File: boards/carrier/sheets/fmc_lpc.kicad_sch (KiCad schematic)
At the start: 3 parts, among them J1 FX10A-168P-SV(91)

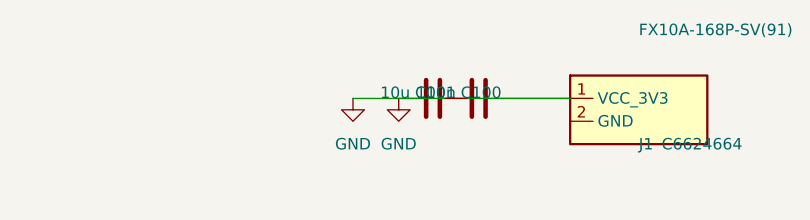
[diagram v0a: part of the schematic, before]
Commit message: Stage 5.5: rotation-derived pin sides + per-edge slot pitch (cluster fix)
Applies the in-flight cluster-fix agent's work (session limit cut its
own commit short). Two architectural changes that close the
sub-sheet wire_dangling / net-merging class of errors:

1) Rotation-derived page-side detection
   (core/layout/geometry.py + core/layout/cluster.py)

   Previously cluster.pin_side() compared abs(pin.x) vs abs(pin.y) on
   the symbol-relative coordinate to guess which body edge a pin
   emerges from. This mis-classified pins on ICs whose pin columns
   span a larger y-range than the body width — FUSB302's seven
   left-column pins (±7.62 mm in y) on a 20 mm-wide body wrap to
   "top/bottom" with the axis-dominance rule, but they're actually
   left-edge pins. The cluster then places passives on the wrong
   side and the resulting wires collide into other nets.

   The new page_side_from_pin() helper derives the page-side from the
   pin's intrinsic KiCad rotation (0 = LEFT edge, 90 = BOTTOM, 180 =
   RIGHT, 270 = TOP) combined with the placed symbol's rotation. This
   is the canonical KiCad convention and doesn't depend on body
   proportions.

   PinGeometry / PinGeometryAbs gain pin_rotation + symbol_rotation
   fields; SymbolGeometryCache reads pin.rotation from the cached
   SymbolDefinition (kicad-sch-api's list_pins() flattens it away).
   pin_side() takes optional pin_rotation/symbol_rotation; falls back
   to the legacy heuristic when not supplied.

2) Per-edge slot pitch
   (core/layout/_constants.py + core/layout/cluster.py)

   LEFT/RIGHT-edge passive swarms fan OUTWARD along the perpendicular
   axis: each slot is one passive body + one power-symbol stub further
   out. The pitch must clear 2 × PASSIVE_PIN_HALF (7.62 mm) +
   POWER_SYMBOL_OFFSET (5.08 mm), so HORIZONTAL_SWARM_PITCH_MM is now
   15.24 mm — was previously the same 5.08 mm used for TOP/BOTTOM, so
   adjacent slots' endpoints collapsed onto one another and KiCad
   merged the entire stack 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
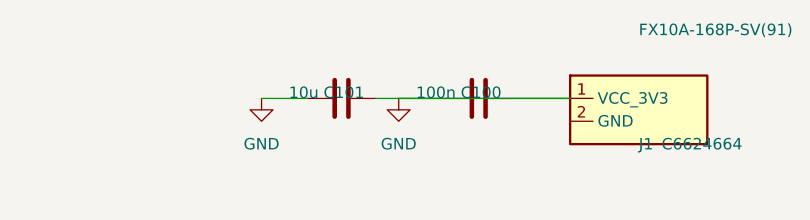
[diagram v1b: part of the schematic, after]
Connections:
- net GND: now also C100.1, C101.1, J1.1 (VCC_3V3)
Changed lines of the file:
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@@
 		(instances
 			(project "FMC LPC Expansion (VITA 57.1 LPC connector)"
-				(path "/fc40dd86-525d-438d-b7ef-e250bfa41e2b"
+				(path "/122dffa9-ed4e-4f88-bbd4-c381f7887d2a"
 					(reference "J1")
 					(unit 1)
@@
 		(instances
 			(project "FMC LPC Expansion (VITA 57.1 LPC connector)"
-				(path "/fc40dd86-525d-438d-b7ef-e250bfa41e2b"
+				(path "/122dffa9-ed4e-4f88-bbd4-c381f7887d2a"
 					(reference "C100")
 					(unit 1)
@@
 		(instances
 			(project "FMC LPC Expansion (VITA 57.1 LPC connector)"
-				(path "/fc40dd86-525d-438d-b7ef-e250bfa41e2b"
+				(path "/122dffa9-ed4e-4f88-bbd4-c381f7887d2a"
 					(reference "#PWR100")
 					(unit 1)
@@
 	(symbol
 		(lib_id "Device:C")
-		(at 213.36 35.56 270)
+		(at 203.2 35.56 270)
 		(unit 1)
 		(exclude_from_sim no)
@@
 		(fields_autoplaced no)
 		(property "Reference" "C101"
-			(at 215.9 34.925 270)
+			(at 205.74 34.925 270)
 			(effects
 				(font
@@
 		)
 		(property "Value" "10u"
-			(at 210.82 34.925 270)
+			(at 200.66 34.925 270)
 			(effects
 				(font
@@
 		)
 		(property "Footprint" "Capacitor_SMD:C_0402_1005Metric"
-			(at 214.3252 31.75 0.0000)
+			(at 204.1652 31.75 0.0000)
 			(effects
 				(font
@@
 		(instances
 			(project "FMC LPC Expansion (VITA 57.1 LPC connector)"
-				(path "/fc40dd86-525d-438d-b7ef-e250bfa41e2b"
+				(path "/122dffa9-ed4e-4f88-bbd4-c381f7887d2a"
 					(reference "C101")
 					(unit 1)
@@
 	(symbol
 		(lib_id "power:GND")
-		(at 204.47 35.56 0)
+		(at 194.31 35.56 0)
 		(unit 1)
 		(exclude_from_sim no)
@@
 		(fields_autoplaced no)
 		(property "Reference" "#PWR101"
-			(at 204.47 29.21 0.0000)
+			(at 194.31 29.21 0.0000)
 			(effects
 				(font
@@
 		)
 		(property "Value" "GND"
-			(at 204.47 40.64 0)
+			(at 194.31 40.64 0)
 			(effects
 				(font
@@
 		)
 		(property "Footprint" ""
-			(at 204.47 35.56 0.0000)
-			(effects
-				(font
-					(size 1.27 1.27)
-				)
-				(hide yes)
-			)
-		)
-		(pin "1"
-		)
-		(instances
-			(project "FMC LPC Expansion (VITA 57.1 LPC connector)"
-				(path "/fc40dd86-525d-438d-b7ef-e250bfa41e2b"
+			(at 194.31 35.56 0.0000)
+			(effects
+				(font
+					(size 1.27 1.27)
+				)
+				(hide yes)
+			)
+		)
+		(pin "1"
+		)
+		(instances
+			(project "FMC LPC Expansion (VITA 57.1 LPC connector)"
+				(path "/122dffa9-ed4e-4f88-bbd4-c381f7887d2a"
 					(reference "#PWR101")
 					(unit 1)
@@
 		(instances
 			(project "FMC LPC Expansion (VITA 57.1 LPC connector)"
-				(path "/fc40dd86-525d-438d-b7ef-e250bfa41e2b"
+				(path "/122dffa9-ed4e-4f88-bbd4-c381f7887d2a"
 					(reference "#PWR102")
 					(unit 1)
@@
 	(wire
 		(pts
-			(xy 228.6 35.56) (xy 217.17 35.56)
+			(xy 228.6 35.56) (xy 207.01 35.56)
 		)
 		(stroke
@@
 	(wire
 		(pts
-			(xy 209.55 35.56) (xy 204.47 35.56)
-		)
-		(stroke
+			(xy 199.39 35.56) (xy 194.31 35.56)
+		)
+		(stroke
